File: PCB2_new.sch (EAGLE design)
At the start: 109 parts

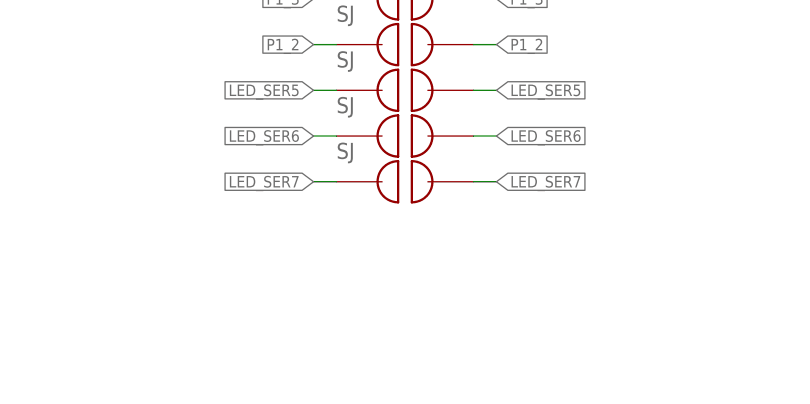
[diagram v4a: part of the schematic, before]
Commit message: Fixed pin distances for PCB2 and added shift register pins to the right side of board
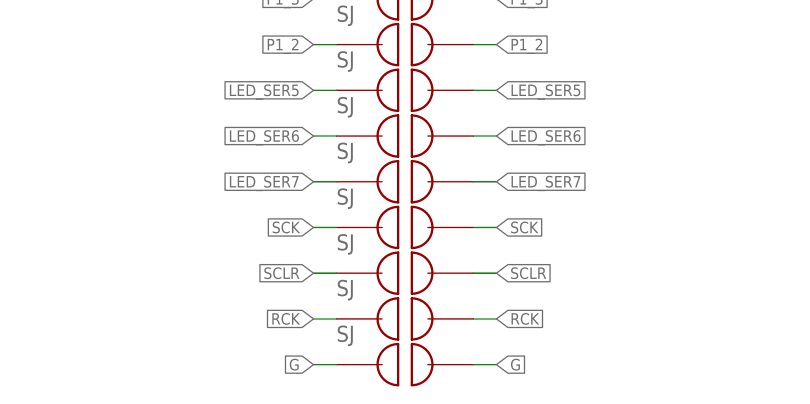
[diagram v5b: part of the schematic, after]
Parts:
- added U$80, U$81, U$82, U$83: JUMPER, ECE477_Guitutar:JUMPER
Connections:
- net G: now also U$83.P$1, U$83.P$2
- net RCK: now also U$82.P$1, U$82.P$2
- net SCK: now also U$80.P$1, U$80.P$2
- net SCLR: now also U$81.P$1, U$81.P$2
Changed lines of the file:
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@@
 <?xml version="1.0" encoding="utf-8"?>
 <!DOCTYPE eagle SYSTEM "eagle.dtd">
-<eagle version="8.1.0">
+<eagle version="8.0.1">
 <drawing>
 <settings>
@@
 <part name="R5" library="rcl" deviceset="R-US_" device="M0805" value="330k"/>
 <part name="R6" library="rcl" deviceset="R-US_" device="M0805" value="330k"/>
+<part name="U$80" library="ECE477_Guitutar" deviceset="JUMPER" device=""/>
+<part name="U$81" library="ECE477_Guitutar" deviceset="JUMPER" device=""/>
+<part name="U$82" library="ECE477_Guitutar" deviceset="JUMPER" device=""/>
+<part name="U$83" library="ECE477_Guitutar" deviceset="JUMPER" device=""/>
 </parts>
 <sheets>
@@
 <instance part="R5" gate="G$1" x="208.28" y="251.46"/>
 <instance part="R6" gate="G$1" x="246.38" y="251.46"/>
+<instance part="U$80" gate="G$1" x="256.54" y="20.32"/>
+<instance part="U$81" gate="G$1" x="256.54" y="15.24"/>
+<instance part="U$82" gate="G$1" x="256.54" y="10.16"/>
+<instance part="U$83" gate="G$1" x="256.54" y="5.08"/>
 </instances>
 <busses>
@@
 <pinref part="U$73" gate="G$1" pin="P$1"/>
 </segment>
+<segment>
+<pinref part="U$83" gate="G$1" pin="P$2"/>
+<wire x1="264.16" y1="5.08" x2="266.7" y2="5.08" width="0.1524" layer="91"/>
+<label x="266.7" y="5.08" size="1.27" layer="95" xref="yes"/>
+</segment>
+<segment>
+<wire x1="248.92" y1="5.08" x2="246.38" y2="5.08" width="0.1524" layer="91"/>
+<label x="246.38" y="5.08" size="1.27" layer="95" rot="R180" xref="yes"/>
+<pinref part="U$83" gate="G$1" pin="P$1"/>
+</segment>
 </net>
 <net name="SCK" class="0">
@@
 <label x="198.12" y="81.28" size="1.27" layer="95" xref="yes"/>
 </segment>
+<segment>
+<wire x1="248.92" y1="20.32" x2="246.38" y2="20.32" width="0.1524" layer="91"/>
+<label x="246.38" y="20.32" size="1.27" layer="95" rot="R180" xref="yes"/>
+<pinref part="U$80" gate="G$1" pin="P$1"/>
+</segment>
+<segment>
+<pinref part="U$80" gate="G$1" pin="P$2"/>
+<wire x1="264.16" y1="20.32" x2="266.7" y2="20.32" width="0.1524" layer="91"/>
+<label x="266.7" y="20.32" size="1.27" layer="95" xref="yes"/>
+</segment>
 </net>
 <net name="RCK" class="0">
@@
 <pinref part="U$72" gate="G$1" pin="P$1"/>
 </segment>
+<segment>
+<pinref part="U$82" gate="G$1" pin="P$2"/>
+<wire x1="264.16" y1="10.16" x2="266.7" y2="10.16" width="0.1524" layer="91"/>
+<label x="266.7" y="10.16" size="1.27" layer="95" xref="yes"/>
+</segment>
+<segment>
+<wire x1="248.92" y1="10.16" x2="246.38" y2="10.16" width="0.1524" layer="91"/>
+<label x="246.38" y="10.16" size="1.27" layer="95" rot="R180" xref="yes"/>
+<pinref part="U$82" gate="G$1" pin="P$1"/>
+</segment>
 </net>
 <net name="N$24" class="0">
@@
 <label x="198.12" y="76.2" size="1.27" layer="95" xref="yes"/>
 </segment>
-</net>
+<segment>
+<wire x1="248.92" y1="15.24" x2="246.38" y2="15.24" width="0.1524" layer="91"/>
+<label x="246.38" y="15.24" size="1.27" layer="95" rot="R180" xref="yes"/>
+<pinref part="U$81" gate="G$1" pin="P$1"/>
+</segment>
+<segment>
+<pinref part="U$81" gate="G$1" pin="P$2"/>
+<wire x1="264.16" y1="15.24" x2="266.7" y2="15.24" width="0.1524" layer="91"/>
+<label x="266.7" y="15.24" size="1.27" layer="95" xref="yes"/>
+</segment>
+</net>
